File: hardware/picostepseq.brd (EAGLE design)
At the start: 123.2 x 54.6 mm, 27 parts, among them J1 SJ-3523-SMT, J2 SJ-3523-SMT, SW1 LED_SWITCHSTEP, SW2 LED_SWITCHSTEP, SW3 LED_SWITCHSTEP, SW4 LED_SWITCHSTEP, SW5 LED_SWITCHSTEP, SW6 LED_SWITCHSTEP, SW7 LED_SWITCHSTEP, SW8 LED_SWITCHSTEP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

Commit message: sigh trs-a/b will kill me
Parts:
- added C1: (no value), rcl:C025-025X050
- moved J1 1.27 mm to (119.8, 44.4)
- moved J2 1.27 mm to (119.8, 33.4)
- moved R1 1.27 mm to (102.3, 47.9)
- moved R2 1.27 mm to (102.3, 45.4)
- moved R3 1.27 mm to (102.3, 42.9)
- moved R4 1.27 mm to (102.3, 40.4)
- moved U2 1.27 mm to (102.3, 33.4)
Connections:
- removed net M_IN: J2.2, R3.2
- removed net M_OUT: J1.2, R1.1
- new net N$13: J1.3, R1.1
- new net N$14: J2.3, R3.2
- net +3V3: now also C1.1
- net GND: now also C1.2
- net N$1: now also J1.2; no longer J1.3
- net N$4: now also J2.2; no longer J2.3
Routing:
- net N$14: track 0.00 -> 21.1 mm
- net N$13: track 0.00 -> 16.4 mm
- net M_IN: track 9.49 -> 0.00 mm
- net N$4: track 14.8 -> 6.55 mm
- net N$1: track 14.7 -> 6.51 mm, vias 0 -> 1
- net M_OUT: track 5.47 -> 0.00 mm
- net MIDI_OUT: track 56.6 -> 55.3 mm
- net MIDI_IN: track 74.1 -> 73.1 mm

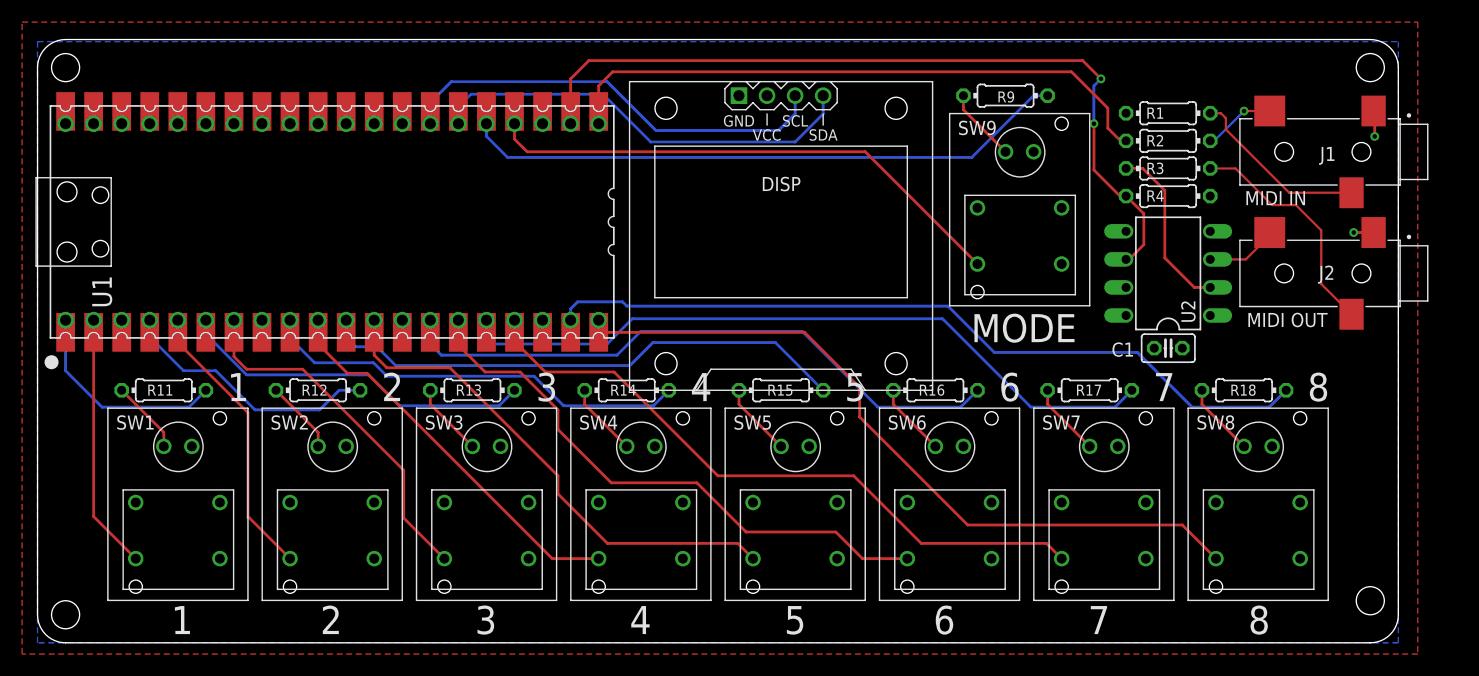
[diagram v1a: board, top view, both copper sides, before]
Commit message: update to knob
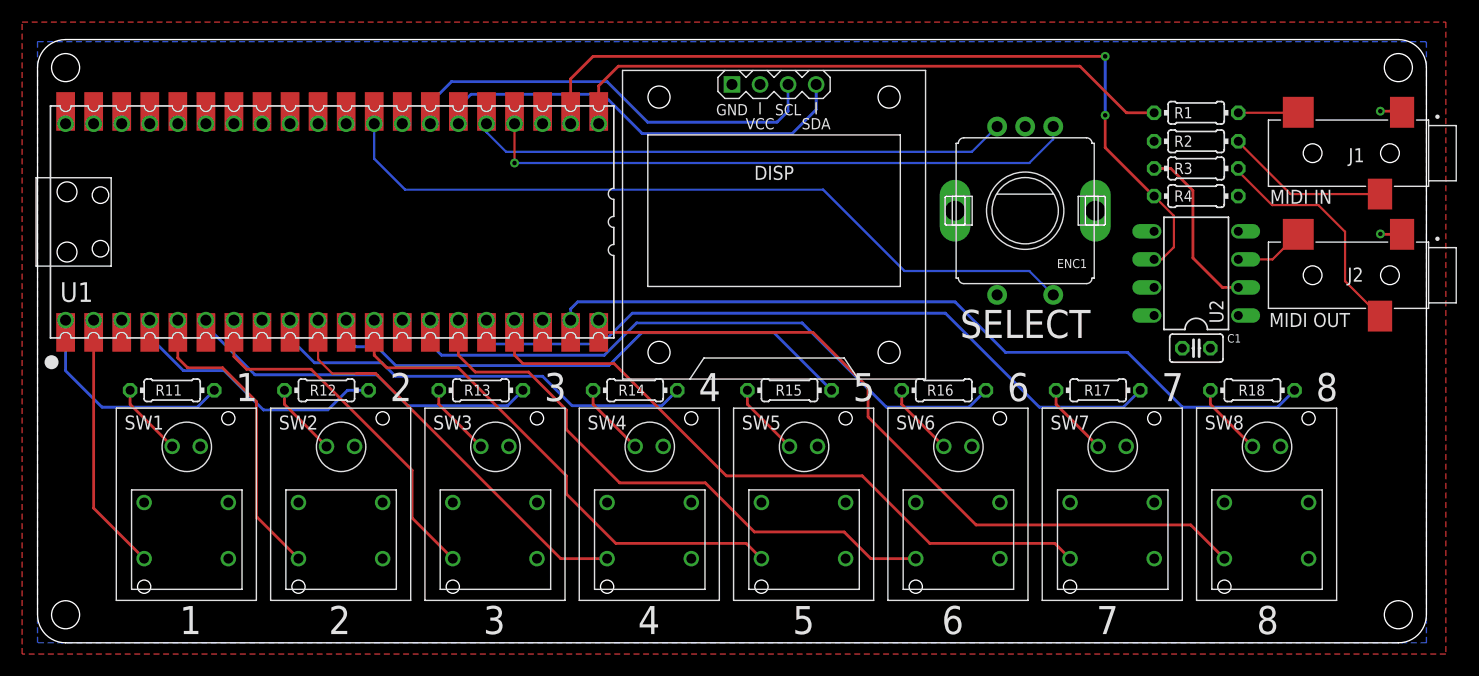
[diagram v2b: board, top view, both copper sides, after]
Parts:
- removed R9: 1k, rcl:0204/7
- removed SW9: LED_SWITCHSTEP, todstuff:LED_SWITCH_STEP
- added ENC1: PEC11, adafruit_electromech:PEC11+SWITCH
- R1: value 33 -> 10
- R2: value 10 -> 33
- moved J2 2.58 mm to (122.4, 33.3)
- moved J1 2.58 mm to (122.4, 44.3)
- moved R1 2.54 mm to (104.9, 48.0)
- moved R2 2.54 mm to (104.9, 45.4)
- moved C1 2.54 mm to (104.9, 26.7)
- moved R3 2.54 mm to (104.9, 42.9)
- moved R4 2.54 mm to (104.9, 40.4)
- moved U2 2.54 mm to (104.9, 33.4)
- moved DISP 1.20 mm to (66.7, 37.8)
- moved R11 0.76 mm to (12.2, 22.9)
- moved R12 0.76 mm to (26.2, 22.9)
- moved R13 0.76 mm to (40.1, 22.9)
- moved R15 0.76 mm to (68.1, 22.9)
- moved R16 0.76 mm to (82.0, 22.9)
- moved R17 0.76 mm to (96.0, 22.9)
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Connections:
- removed net LED9: R9.2, U1.25, U1.P$25
- removed net N$3: R9.1, SW9.5
- removed net SW9: SW9.2, U1.24, U1.P$24
- new net ROTA: ENC1.P$A, U1.24, U1.P$24
- new net ROTB: ENC1.P$B, U1.25, U1.P$25
- new net ROTSW: ENC1.P$1, U1.29, U1.P$29
- net +3V3: now also R2.2; no longer R1.2
- net GND: now also ENC1.P$2, ENC1.P$C, ENC1.P$GND1, ENC1.P$GND2; no longer SW9.1_B, SW9.6
- net MIDI_OUT: now also R1.2; no longer R2.2
- net N$1: now also R1.1; no longer R2.1
- net N$13: now also R2.1; no longer R1.1
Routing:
- net ROTSW: track 0.00 -> 70.9 mm
- net ROTA: track 0.00 -> 56.6 mm, vias 0 -> 1
- net LED9: track 56.2 -> 0.00 mm
- net ROTB: track 0.00 -> 49.8 mm
- net SW9: track 49.1 -> 0.00 mm
- net N$3: track 6.66 -> 0.00 mm
- net GND: track 15.4 -> 12.9 mm
- net MIDI_IN: track 73.1 -> 75.4 mm
- net SW2: track 25.8 -> 28.0 mm
- net SW4: track 35.6 -> 37.2 mm
- net N$13: track 16.4 -> 14.8 mm
- net SW7: track 59.6 -> 61.1 mm
- net LED5: track 49.5 -> 51.0 mm
- net LED6: track 57.6 -> 59.0 mm
- net SW6: track 52.0 -> 53.2 mm
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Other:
- board size 123.2 x 54.6 mm -> 125.7 x 54.6 mm
- board text added: "J1,2: CUI SJ-3523-SMT"
- board text added: "R1:33, R2:10, R3:220, C1: 100n"
- board text added: "SELECT"
- board text removed: "J1,2: SJ-3523-SMT"
- board text removed: "MODE"
- board text removed: "R1:33, R2:10, R3:220"
